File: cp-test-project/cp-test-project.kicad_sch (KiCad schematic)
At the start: 0 parts

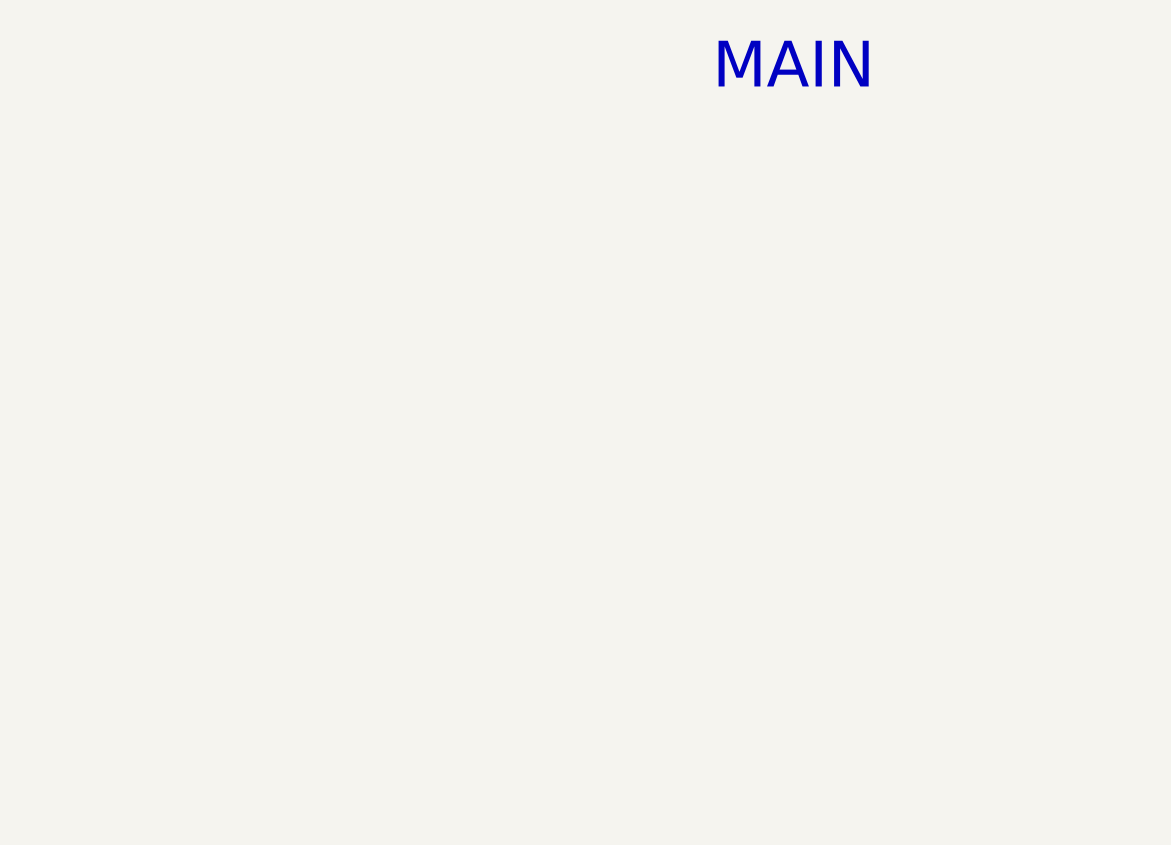
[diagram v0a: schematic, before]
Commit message: updated to hierarchical
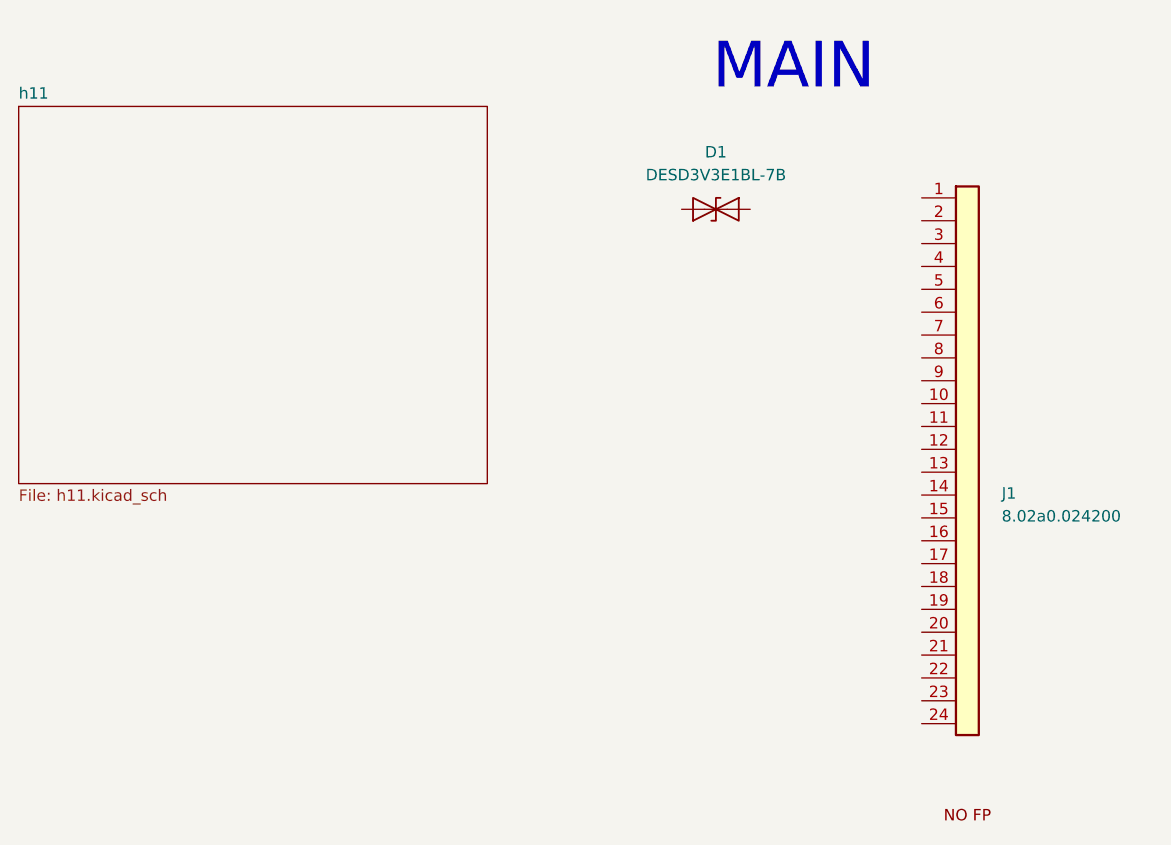
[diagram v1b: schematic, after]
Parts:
- added D1: DESD3V3E1BL-7B, AW:CR_X1-DFN1006-2_DIO-M, symbol AW:DESD3V3E1BL-7B
- added J1: 8.02a0.024200, symbol AW:GDEW0154M09
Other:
- added sheet h11 (h11.kicad_sch)
